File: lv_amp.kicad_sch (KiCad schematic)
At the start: 81 parts, among them J1 Jack-DC, J2 AudioJack2, J3 AudioJack2, Q1 Q_NMOS_DGS, U1 MAX1771xSA, U2 TL072, U3 ECC83, U4 ECC83, U5 ECC83

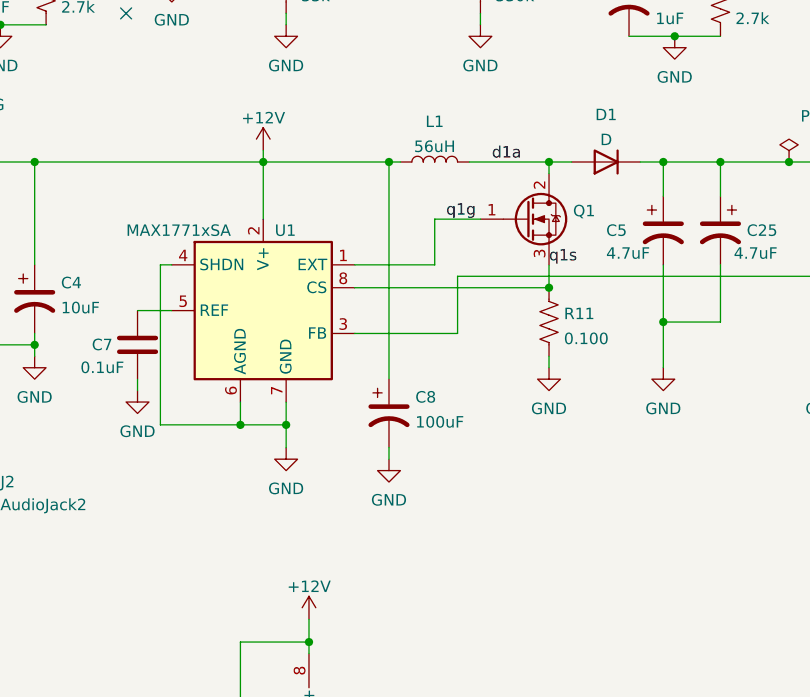
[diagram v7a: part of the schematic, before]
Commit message: alpha0 errata: more input filtering on inductor
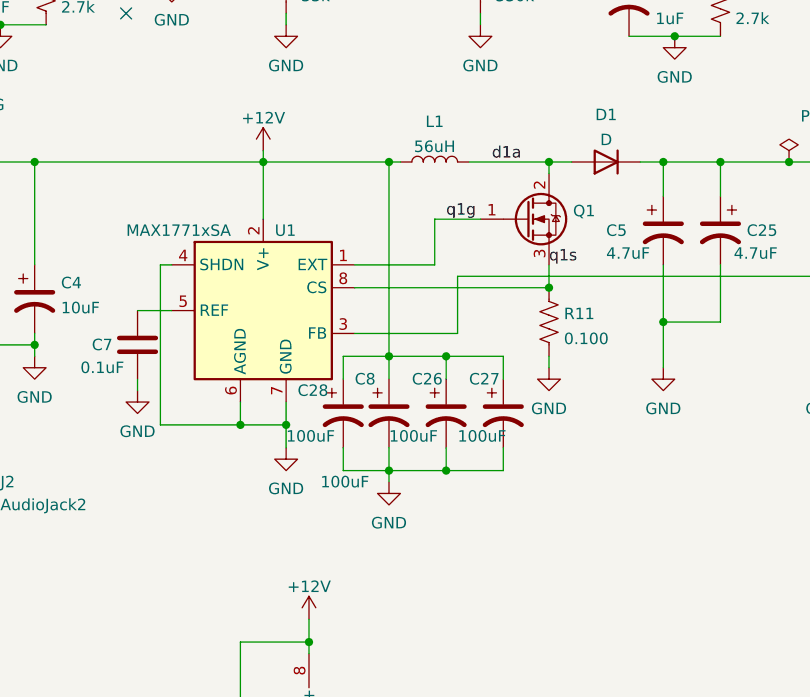
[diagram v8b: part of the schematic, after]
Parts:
- added C26, C27, C28: 100uF, Capacitor_Tantalum_SMD:CP_EIA-7343-43_Kemet-X, symbol Device:C_Polarized_US
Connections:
- net +12V: now also C26.1, C27.1, C28.1
- net GND: now also C26.2, C27.2, C28.2
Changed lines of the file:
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@@
   (junction (at 95.25 82.55) (diameter 0) (color 0 0 0 0)
   )
+  (junction (at 170.18 140.97) (diameter 0) (color 0 0 0 0)
+  )
   (junction (at 254 76.2) (diameter 0) (color 0 0 0 0)
   )
@@
   (junction (at 212.09 132.08) (diameter 0) (color 0 0 0 0)
   )
+  (junction (at 163.83 153.67) (diameter 0) (color 0 0 0 0)
+  )
   (junction (at 173.99 82.55) (diameter 0) (color 0 0 0 0)
   )
@@
   (junction (at 59.69 72.39) (diameter 0) (color 0 0 0 0)
   )
+  (junction (at 163.83 140.97) (diameter 0) (color 0 0 0 0)
+  )
   (junction (at 62.23 105.41) (diameter 0) (color 0 0 0 0)
   )
@@
   (junction (at 154.94 189.23) (diameter 0) (color 0 0 0 0)
   )
+  (junction (at 170.18 153.67) (diameter 0) (color 0 0 0 0)
+  )
   (junction (at 73.66 72.39) (diameter 0) (color 0 0 0 0)
   )
@@
     (stroke (width 0) (type default) (color 0 0 0 0))
   )
+  (wire (pts (xy 163.83 153.67) (xy 163.83 154.94))
+    (stroke (width 0) (type default) (color 0 0 0 0))
+  )
   (wire (pts (xy 24.13 83.82) (xy 35.56 83.82))
     (stroke (width 0) (type default) (color 0 0 0 0))
@@
     (stroke (width 0) (type default) (color 0 0 0 0))
   )
+  (wire (pts (xy 176.53 153.67) (xy 170.18 153.67))
+    (stroke (width 0) (type default) (color 0 0 0 0))
+  )
   (wire (pts (xy 85.09 76.2) (xy 85.09 78.74))
     (stroke (width 0) (type default) (color 0 0 0 0))
@@
     (stroke (width 0) (type default) (color 0 0 0 0))
   )
+  (wire (pts (xy 158.75 143.51) (xy 158.75 140.97))
+    (stroke (width 0) (type default) (color 0 0 0 0))
+  )
   (wire (pts (xy 95.25 82.55) (xy 99.06 82.55))
     (stroke (width 0) (type default) (color 0 0 0 0))
@@
     (stroke (width 0) (type default) (color 0 0 0 0))
   )
+  (wire (pts (xy 176.53 151.13) (xy 176.53 153.67))
+    (stroke (width 0) (type default) (color 0 0 0 0))
+  )
   (wire (pts (xy 57.15 105.41) (xy 62.23 105.41))
     (stroke (width 0) (type default) (color 0 0 0 0))
@@
     (stroke (width 0) (type default) (color 0 0 0 0))
   )
+  (wire (pts (xy 163.83 153.67) (xy 170.18 153.67))
+    (stroke (width 0) (type default) (color 0 0 0 0))
+  )
   (wire (pts (xy 107.95 119.38) (xy 109.22 119.38))
     (stroke (width 0) (type default) (color 0 0 0 0))
@@
     (stroke (width 0) (type default) (color 0 0 0 0))
   )
+  (wire (pts (xy 158.75 140.97) (xy 163.83 140.97))
+    (stroke (width 0) (type default) (color 0 0 0 0))
+  )
   (wire (pts (xy 242.57 53.34) (xy 242.57 69.85))
     (stroke (width 0) (type default) (color 0 0 0 0))
@@
     (stroke (width 0) (type default) (color 0 0 0 0))
   )
+  (wire (pts (xy 163.83 140.97) (xy 170.18 140.97))
+    (stroke (width 0) (type default) (color 0 0 0 0))
+  )
+  (wire (pts (xy 163.83 140.97) (xy 163.83 143.51))
+    (stroke (width 0) (type default) (color 0 0 0 0))
+  )
   (wire (pts (xy 245.11 138.43) (xy 247.65 138.43))
     (stroke (width 0) (type default) (color 0 0 0 0))
@@
     (stroke (width 0) (type default) (color 0 0 0 0))
   )
+  (wire (pts (xy 170.18 151.13) (xy 170.18 153.67))
+    (stroke (width 0) (type default) (color 0 0 0 0))
+  )
   (wire (pts (xy 212.09 140.97) (xy 212.09 142.24))
     (stroke (width 0) (type default) (color 0 0 0 0))
@@
     (stroke (width 0) (type default) (color 0 0 0 0))
   )
+  (wire (pts (xy 158.75 153.67) (xy 163.83 153.67))
+    (stroke (width 0) (type default) (color 0 0 0 0))
+  )
   (wire (pts (xy 232.41 80.01) (xy 234.95 80.01))
     (stroke (width 0) (type default) (color 0 0 0 0))
@@
     (stroke (width 0) (type default) (color 0 0 0 0))
   )
-  (wire (pts (xy 163.83 119.38) (xy 163.83 143.51))
+  (wire (pts (xy 163.83 119.38) (xy 163.83 140.97))
     (stroke (width 0) (type default) (color 0 0 0 0))
   )
@@
     (stroke (width 0) (type default) (color 0 0 0 0))
   )
+  (wire (pts (xy 158.75 151.13) (xy 158.75 153.67))
+    (stroke (width 0) (type default) (color 0 0 0 0))
+  )
   (wire (pts (xy 254 85.09) (xy 254 87.63))
     (stroke (width 0) (type default) (color 0 0 0 0))
@@
     (stroke (width 0) (type default) (color 0 0 0 0))
   )
-  (wire (pts (xy 163.83 151.13) (xy 163.83 152.4))
+  (wire (pts (xy 163.83 151.13) (xy 163.83 153.67))
     (stroke (width 0) (type default) (color 0 0 0 0))
   )
@@
     (stroke (width 0) (type default) (color 0 0 0 0))
   )
+  (wire (pts (xy 170.18 140.97) (xy 170.18 143.51))
+    (stroke (width 0) (type default) (color 0 0 0 0))
+  )
+  (wire (pts (xy 170.18 140.97) (xy 176.53 140.97))
+    (stroke (width 0) (type default) (color 0 0 0 0))
+  )
   (wire (pts (xy 29.21 163.83) (xy 29.21 168.91))
     (stroke (width 0) (type default) (color 0 0 0 0))
@@
     (stroke (width 0) (type default) (color 0 0 0 0))
   )
+  (wire (pts (xy 176.53 140.97) (xy 176.53 143.51))
+    (stroke (width 0) (type default) (color 0 0 0 0))
+  )
   (wire (pts (xy 220.98 119.38) (xy 227.33 119.38))
     (stroke (width 0) (type default) (color 0 0 0 0))
@@
     (pin "1")
   )
+  (symbol (lib_id "Device:C_Polarized_US") (at 176.53 147.32 0) (unit 1)
+    (in_bom yes) (on_board yes)
+    (property "Reference" "C27" (id 0) (at 172.72 143.51 0)
+      (effects (font (size 1.27 1.27)) (justify left))
+    )
+    (property "Value" "100uF" (id 1) (at 171.45 149.86 0)
+      (effects (font (size 1.27 1.27)) (justify left))
+    )
+    (property "Footprint" "Capacitor_Tantalum_SMD:CP_EIA-7343-43_Kemet-X" (id 2) (at 176.53 147.32 0)
+      (effects (font (size 1.27 1.27)) hide)
+    )
+    (property "Datasheet" "~" (id 3) (at 176.53 147.32 0)
+      (effects (font (size 1.27 1.27)) hide)
+    )
+    (pin "1")
+    (pin "2")
+  )
   (symbol (lib_id "power:GND") (at 27.94 81.28 90) (unit 1)
     (in_bom yes) (on_board yes) (fields_autoplaced)
@@
     (pin "7")
   )
+  (symbol (lib_id "Device:C_Polarized_US") (at 170.18 147.32 0) (unit 1)
+    (in_bom yes) (on_board yes)
+    (property "Reference" "C26" (id 0) (at 166.37 143.51 0)
+      (effects (font (size 1.27 1.27)) (justify left))
+    )
+    (property "Value" "100uF" (id 1) (at 163.83 149.86 0)
+      (effects (font (size 1.27 1.27)) (justify left))
+    )
+    (property "Footprint" "Capacitor_Tantalum_SMD:CP_EIA-7343-43_Kemet-X" (id 2) (at 170.18 147.32 0)
+      (effects (font (size 1.27 1.27)) hide)
+    )
+    (property "Datasheet" "~" (id 3) (at 170.18 147.32 0)
+      (effects (font (size 1.27 1.27)) hide)
+    )
+    (pin "1")
+    (pin "2")
+  )
   (symbol (lib_id "Device:R_US") (at 154.94 64.77 0) (unit 1)
     (in_bom yes) (on_board yes)
@@
     (pin "2")
   )
-  (symbol (lib_id "power:GND") (at 163.83 152.4 0) (unit 1)
+  (symbol (lib_id "power:GND") (at 163.83 154.94 0) (unit 1)
     (in_bom yes) (on_board yes) (fields_autoplaced)
-    (property "Reference" "#PWR031" (id 0) (at 163.83 158.75 0)
+    (property "Reference" "#PWR031" (id 0) (at 163.83 161.29 0)
       (effects (font (size 1.27 1.27)) hide)
     )
-    (property "Value" "GND" (id 1) (at 163.83 156.9625 0))
-    (property "Footprint" "" (id 2) (at 163.83 152.4 0)
+    (property "Value" "GND" (id 1) (at 163.83 159.5025 0))
+    (property "Footprint" "" (id 2) (at 163.83 154.94 0)
       (effects (font (size 1.27 1.27)) hide)
     )
-    (property "Datasheet" "" (id 3) (at 163.83 152.4 0)
+    (property "Datasheet" "" (id 3) (at 163.83 154.94 0)
       (effects (font (size 1.27 1.27)) hide)
     )
@@
     (pin "2")
   )
+  (symbol (lib_id "Device:C_Polarized_US") (at 158.75 147.32 0) (unit 1)
+    (in_bom yes) (on_board yes)
+    (property "Reference" "C28" (id 0) (at 153.67 144.78 0)
+      (effects (font (size 1.27 1.27)) (justify left))
+    )
+    (property "Value" "100uF" (id 1) (at 152.4 149.86 0)
+      (effects (font (size 1.27 1.27)) (justify left))
+    )
+    (property "Footprint" "Capacitor_Tantalum_SMD:CP_EIA-7343-43_Kemet-X" (id 2) (at 158.75 147.32 0)
+      (effects (font (size 1.27 1.27)) hide)
+    )
+    (property "Datasheet" "~" (id 3) (at 158.75 147.32 0)
+      (effects (font (size 1.27 1.27)) hide)
+    )
+    (pin "1")
+    (pin "2")
+  )
   (symbol (lib_id "Device:C") (at 68.58 72.39 90) (unit 1)
     (in_bom yes) (on_board yes) (fields_autoplaced)
@@
   )
   (symbol (lib_id "Device:C_Polarized_US") (at 163.83 147.32 0) (unit 1)
-    (in_bom yes) (on_board yes) (fields_autoplaced)
-    (property "Reference" "C8" (id 0) (at 166.751 145.5225 0)
+    (in_bom yes) (on_board yes)
+    (property "Reference" "C8" (id 0) (at 160.02 143.51 0)
       (effects (font (size 1.27 1.27)) (justify left))
     )
-    (property "Value" "100uF" (id 1) (at 166.751 148.2976 0)
+    (property "Value" "100uF" (id 1) (at 156.21 154.94 0)
       (effects (font (size 1.27 1.27)) (justify left))
     )
@@
       (reference "C25") (unit 1) (value "4.7uF") (footprint "Capacitor_SMD:CP_Elec_10x10")
     )
+    (path "/222a1c0d-2693-4802-ada8-5b0adcf96f0c"
+      (reference "C26") (unit 1) (value "100uF") (footprint "Capacitor_Tantalum_SMD:CP_EIA-7343-43_Kemet-X")
+    )
+    (path "/1101c0f6-8dbe-4918-8a41-a923a2979ce2"
+      (reference "C27") (unit 1) (value "100uF") (footprint "Capacitor_Tantalum_SMD:CP_EIA-7343-43_Kemet-X")
+    )
+    (path "/32c162aa-5377-4661-ae1f-a30e5691e542"
+      (reference "C28") (unit 1) (value "100uF") (footprint "Capacitor_Tantalum_SMD:CP_EIA-7343-43_Kemet-X")
+    )
     (path "/3b57d871-c725-4716-ad9b-2bb76745f388"
